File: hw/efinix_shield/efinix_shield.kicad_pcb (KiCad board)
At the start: 2 copper layers, 12 parts, among them J1 DB15_Female_HighDensity_Mount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, J3 Conn_02x18_Odd_Even, U1 MAX3421E, U2 CP2102N-Axx-xQFN24

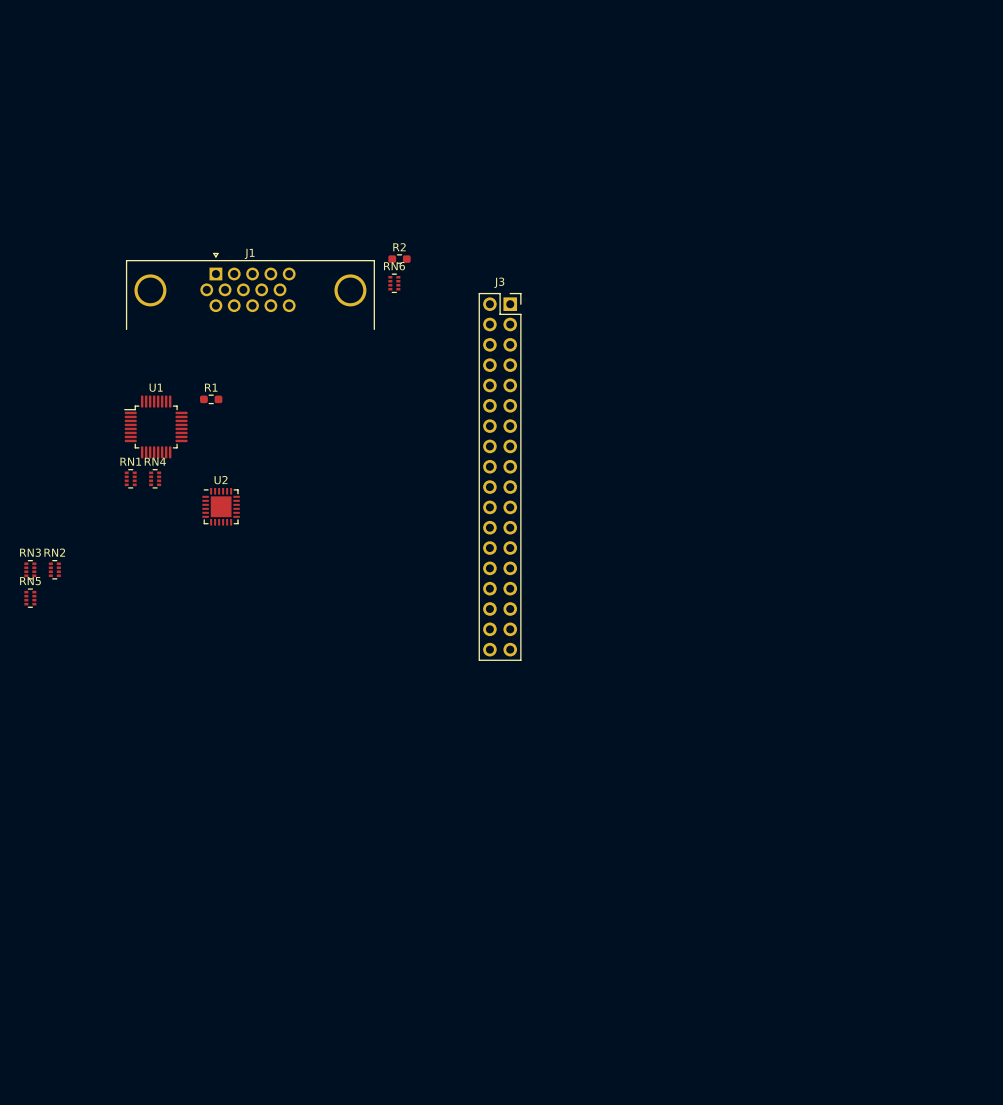
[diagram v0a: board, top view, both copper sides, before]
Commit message: throw some stuff on.
This will have to be changed, some things like the VGA connector will
not work because they will interfere with the cpu adapter.

It may be worth thinking about making these smaller and not including
the ethernet for example, since that will not come for a while.

The only things we really need to start are the SD card and serial port.
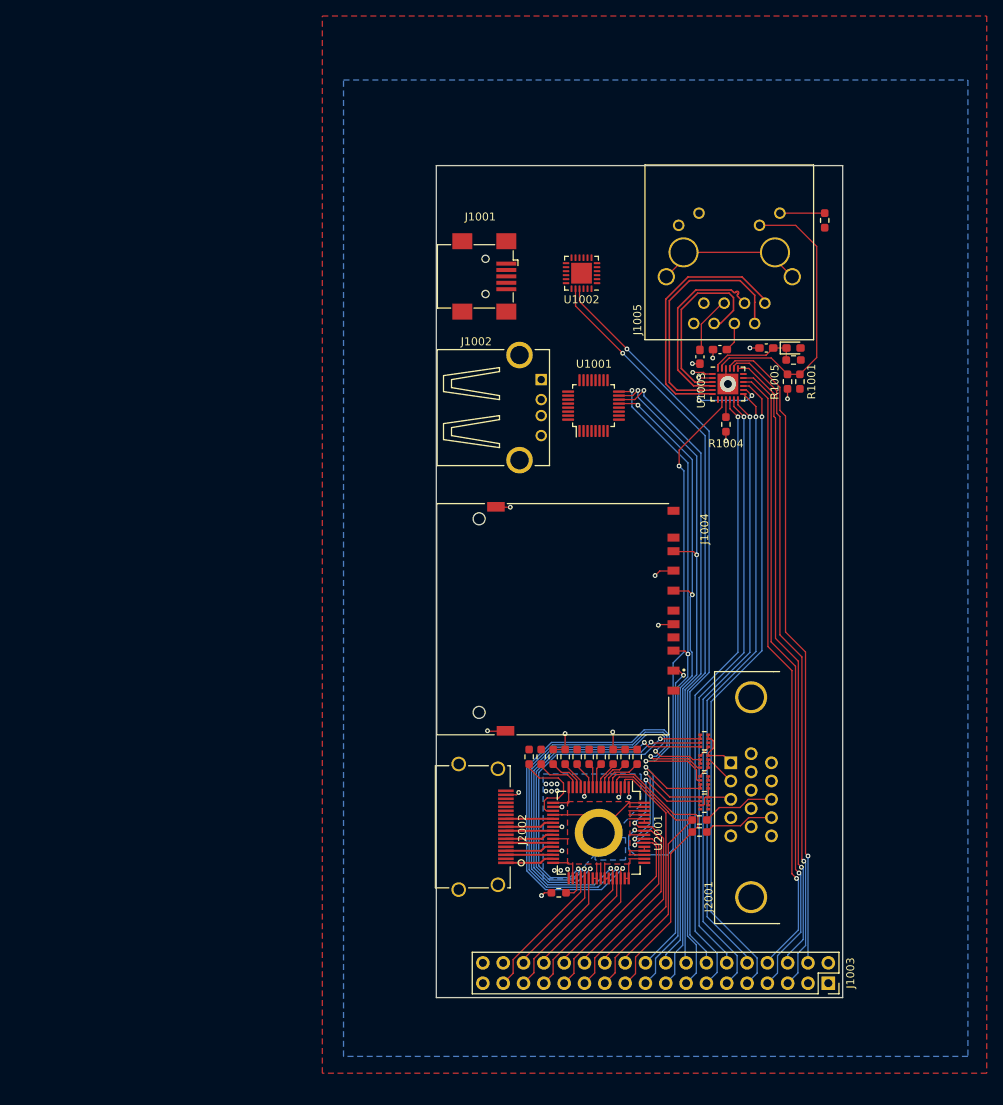
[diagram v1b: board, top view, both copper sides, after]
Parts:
- removed J1: DB15_Female_HighDensity_MountingHoles, Connector_Dsub:DSUB-15-HD_Male_Horizontal_P2.29x1.98mm_EdgePinOffset3.03mm_Housed_MountingHolesOffset4.94mm
- removed R1, R2: 120, Resistor_SMD:R_0603_1608Metric_Pad0.98x0.95mm_HandSolder
- removed RN1, RN2, RN5: 1k, Resistor_SMD:R_Array_Concave_4x0402
- removed RN3, RN4, RN6: 2k, Resistor_SMD:R_Array_Concave_4x0402
- added C1001: 0.1u, Capacitor_SMD:C_0603_1608Metric_Pad1.08x0.95mm_HandSolder, F.Cu at (193.9, 71.4)
- added C1002: 0.1u, Capacitor_SMD:C_0603_1608Metric_Pad1.08x0.95mm_HandSolder, F.Cu at (196.4, 70.5)
- added C1003: 10u, Capacitor_SMD:C_0603_1608Metric_Pad1.08x0.95mm_HandSolder, F.Cu at (202.2, 70.3)
- added D1001: 1N4148, Diode_SMD:D_0603_1608Metric_Pad1.05x0.95mm_HandSolder, F.Cu at (205.7, 70.3)
- added J1001: USB_B_Mini, Connector_USB:USB_Mini-B_Wuerth_65100516121_Horizontal, F.Cu at (167.2, 61.4)
- added J1002: USB_A, Connector_USB:FCI_87520-0010BLF, F.Cu at (171.4, 77.8)
- added J1004: 10067847-001RLF, Connector_Card:AMPHENOL_10067847-001RLF, F.Cu at (166.3, 103.8)
- added J1005: JX0011D21NL, Connector_RJ:JX0011D21NL, F.Cu at (202.1, 64.7)
- added J2001: VGA, Connector_Dsub:ICD15S13E4GX00LF, F.Cu at (200.4, 138.9)
- added J2002: HDMI_A, Connector_HDMI:10029449-111RLF, F.Cu at (169.7, 134.7)
- added R1001: 4k7, Resistor_SMD:R_0603_1608Metric_Pad0.98x0.95mm_HandSolder, F.Cu at (206.4, 74.5)
- added R1002: 10k, Resistor_SMD:R_0603_1608Metric_Pad0.98x0.95mm_HandSolder, F.Cu at (205.7, 71.8)
- added R1003: 220, Resistor_SMD:R_0603_1608Metric_Pad0.98x0.95mm_HandSolder, F.Cu at (209.6, 54.4)
- added R1004: 6.49k 1%, Resistor_SMD:R_0603_1608Metric_Pad0.98x0.95mm_HandSolder, F.Cu at (197.2, 79.8)
- added R1005: 1k, Resistor_SMD:R_0603_1608Metric_Pad0.98x0.95mm_HandSolder, F.Cu at (204.9, 74.5)
- added R2001: 500, Resistor_SMD:R_0603_1608Metric_Pad0.98x0.95mm_HandSolder, F.Cu at (172.6, 121.4)
- added R2002: 120, Resistor_SMD:R_0603_1608Metric_Pad0.98x0.95mm_HandSolder, F.Cu at (193.9, 129.3)
- added R2003: 120, Resistor_SMD:R_0603_1608Metric_Pad0.98x0.95mm_HandSolder, F.Cu at (193.9, 130.8)
- added R2004: 10k, Resistor_SMD:R_0603_1608Metric_Pad0.98x0.95mm_HandSolder, F.Cu at (181.6, 121.4)
- added R2005: 10k, Resistor_SMD:R_0603_1608Metric_Pad0.98x0.95mm_HandSolder, F.Cu at (176.3, 138.4)
- added R2006: 10k, Resistor_SMD:R_0603_1608Metric_Pad0.98x0.95mm_HandSolder, F.Cu at (178.6, 121.4)
- added R2007: 10k, Resistor_SMD:R_0603_1608Metric_Pad0.98x0.95mm_HandSolder, F.Cu at (180.1, 121.4)
- added R2008: 10k, Resistor_SMD:R_0603_1608Metric_Pad0.98x0.95mm_HandSolder, F.Cu at (177.1, 121.4)
- added R2009: 10k, Resistor_SMD:R_0603_1608Metric_Pad0.98x0.95mm_HandSolder, F.Cu at (183.1, 121.4)
- added R2010: 10k, Resistor_SMD:R_0603_1608Metric_Pad0.98x0.95mm_HandSolder, F.Cu at (184.6, 121.4)
- added R2011: 10k, Resistor_SMD:R_0603_1608Metric_Pad0.98x0.95mm_HandSolder, F.Cu at (186.1, 121.4)
- added R2012: 10k, Resistor_SMD:R_0603_1608Metric_Pad0.98x0.95mm_HandSolder, F.Cu at (174.1, 121.4)
- added R2013: 10k, Resistor_SMD:R_0603_1608Metric_Pad0.98x0.95mm_HandSolder, F.Cu at (175.6, 121.4)
- added RN2001: 1k, Resistor_SMD:R_Array_Concave_4x0402, F.Cu at (194.5, 119.4)
- added RN2002: 1k, Resistor_SMD:R_Array_Concave_4x0402, F.Cu at (194.5, 122.0)
- added RN2003: 1k, Resistor_SMD:R_Array_Concave_4x0402, F.Cu at (194.5, 124.6)
- added RN2004: 1k, Resistor_SMD:R_Array_Concave_4x0402, F.Cu at (194.5, 127.2)
- added U1003: KSZ8081RNA, Package_DFN_QFN:QFN-24-1EP_4x4mm_P0.5mm_EP2.6x2.6mm, F.Cu at (197.4, 74.8)
- added U2001: TFP410PAP, Package_QFP:HTQFP-64-1EP_10x10mm_P0.5mm_EP8x8mm_Mask4.4x4.4mm_ThermalVias, F.Cu at (181.3, 130.9)
- moved J1003 93.7 mm to (210.0, 149.7), turned to -90 degrees
- moved U1001 54.7 mm to (180.7, 77.5), turned to 90 degrees
- moved U1002 53.7 mm to (179.2, 61.0), turned to 180 degrees
- renumbered J3 to J1003, U1 to U1001, U2 to U1002
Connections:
- net VDD renamed +3V3
- J1003 pad 10: unconnected-(J3-Pad10) -> /RMII_RXD0
- J1003 pad 11: unconnected-(J3-Pad11) -> /RMII_RXD1
- J1003 pad 12: unconnected-(J3-Pad12) -> /MDCLK
- J1003 pad 13: unconnected-(J3-Pad13) -> /MDIO
- J1003 pad 14: unconnected-(J3-Pad14) -> /UART_RX
- J1003 pad 15: unconnected-(J3-Pad15) -> /UART_TX
- J1003 pad 16: unconnected-(J3-Pad16) -> /SPI_USB_CS
- J1003 pad 17: unconnected-(J3-Pad17) -> /SPI_MISO
- J1003 pad 18: unconnected-(J3-Pad18) -> /SPI_CLK
- J1003 pad 19: unconnected-(J3-Pad19) -> /SPI_MOSI
- J1003 pad 20: unconnected-(J3-Pad20) -> /SPI_SD_CS
- J1003 pad 21: unconnected-(J3-Pad21) -> /VGA_VS
- J1003 pad 22: unconnected-(J3-Pad22) -> /VGA_HS
- J1003 pad 23: unconnected-(J3-Pad23) -> /DVI_DE
- J1003 pad 24: unconnected-(J3-Pad24) -> /VGA_BLUE_0
- J1003 pad 25: unconnected-(J3-Pad25) -> /DVI_CLK
- J1003 pad 26: unconnected-(J3-Pad26) -> /VGA_BLUE_1
- J1003 pad 27: unconnected-(J3-Pad27) -> /VGA_BLUE_2
- J1003 pad 28: unconnected-(J3-Pad28) -> /VGA_GREEN_0
- J1003 pad 29: unconnected-(J3-Pad29) -> /VGA_GREEN_1
- J1003 pad 3: unconnected-(J3-Pad3) -> /SPI_CS_3
- J1003 pad 30: unconnected-(J3-Pad30) -> /VGA_GREEN_2
- J1003 pad 31: unconnected-(J3-Pad31) -> /VGA_RED_0
- J1003 pad 32: unconnected-(J3-Pad32) -> /VGA_RED_1
- J1003 pad 33: unconnected-(J3-Pad33) -> /VGA_RED_2
- J1003 pad 4: unconnected-(J3-Pad4) -> /RMII_TXD1
- J1003 pad 5: unconnected-(J3-Pad5) -> /RMII_TXD0
- J1003 pad 6: unconnected-(J3-Pad6) -> /RMII_TX_EN
- J1003 pad 7: unconnected-(J3-Pad7) -> /RMII_RX_ERR
- J1003 pad 8: unconnected-(J3-Pad8) -> /RMII_CLK_REF
- J1003 pad 9: unconnected-(J3-Pad9) -> /RMII_CRS_DV
- U1001 pad 13: unconnected-(U1-Pad13) -> /SPI_CLK
- U1001 pad 14: unconnected-(U1-Pad14) -> /SPI_USB_CS
- U1001 pad 15: unconnected-(U1-Pad15) -> /SPI_MISO
- U1001 pad 16: unconnected-(U1-Pad16) -> /SPI_MOSI
- U1002 pad 20: unconnected-(U2-Pad20) -> /UART_TX
- U1002 pad 21: unconnected-(U2-Pad21) -> /UART_RX
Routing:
- net /UART_TX: track 0.00 -> 95.4 mm, vias 0 -> 1
- net /DVI_CLK: track 0.00 -> 93.6 mm, vias 0 -> 2
- net /UART_RX: track 0.00 -> 92.8 mm, vias 0 -> 1
- net /SPI_MISO: track 0.00 -> 84.5 mm, vias 0 -> 2
- net /RMII_TXD0: track 0.00 -> 83.7 mm, vias 0 -> 1
- net /SPI_MOSI: track 0.00 -> 82.9 mm, vias 0 -> 2
- net /RMII_TXD1: track 0.00 -> 81.6 mm, vias 0 -> 1
- net /RMII_CRS_DV: track 0.00 -> 81.6 mm, vias 0 -> 1
- net /RMII_RX_ERR: track 0.00 -> 81.1 mm, vias 0 -> 1
- net /RMII_TX_EN: track 0.00 -> 79.3 mm, vias 0 -> 1
- net /SPI_CLK: track 0.00 -> 79.1 mm, vias 0 -> 2
- net /SPI_USB_CS: track 0.00 -> 79.0 mm, vias 0 -> 1
- net /RMII_RXD1: track 0.00 -> 78.3 mm, vias 0 -> 1
- net /RMII_CLK_REF: track 0.00 -> 77.7 mm, vias 0 -> 1
- net /MDIO: track 0.00 -> 77.3 mm, vias 0 -> 1
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- added copper zone on B.Cu, net +3V3
- added copper zone on F.Cu, net +3V3
- added copper zone on B.Cu, net GND
- added copper zone on F.Cu, net GND
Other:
- board outline added: 50.8 x 104 mm

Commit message: Start work on simpler board
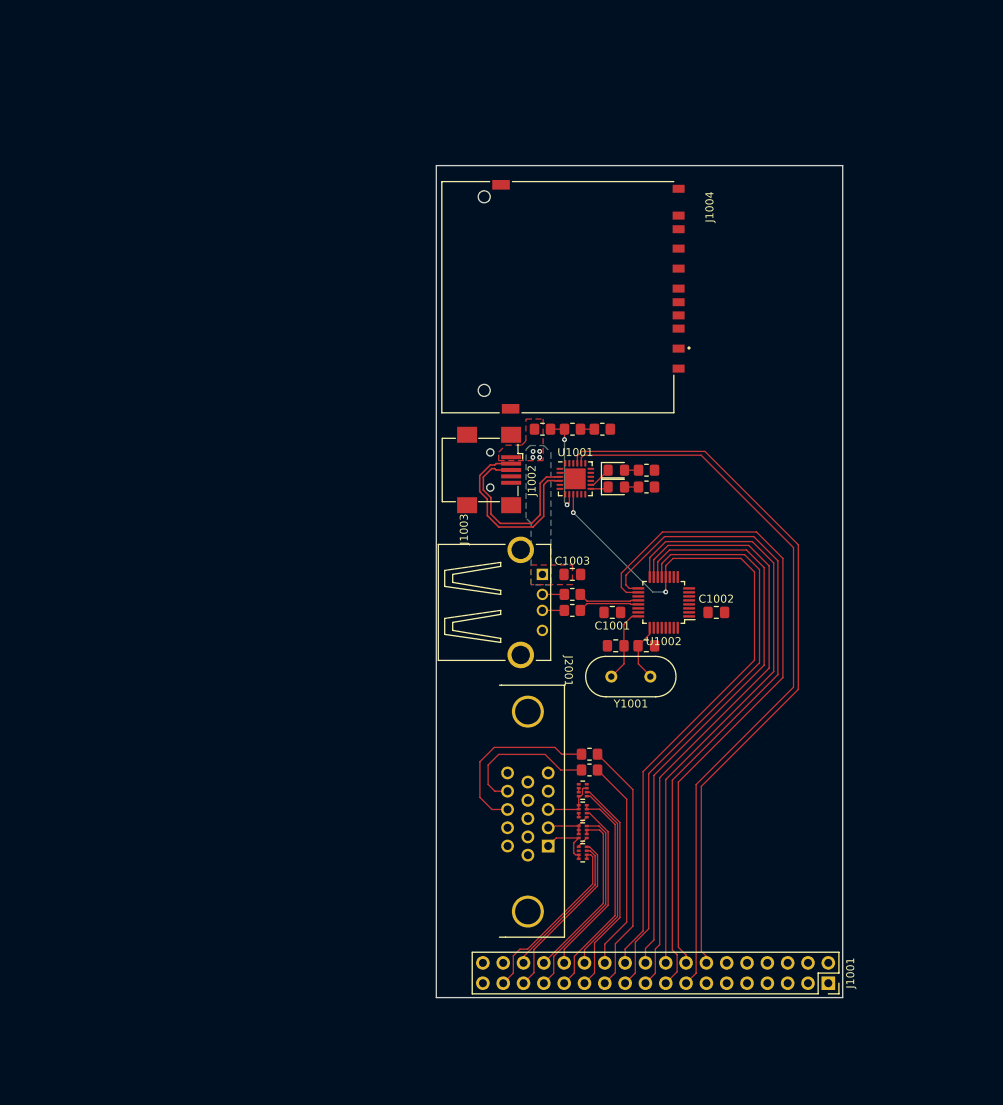
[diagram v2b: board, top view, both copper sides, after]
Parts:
- removed the J1001 at (167.2, 61.4)
- removed J1005: JX0011D21NL, Connector_RJ:JX0011D21NL
- removed J2002: HDMI_A, Connector_HDMI:10029449-111RLF
- removed R2003: 120, Resistor_SMD:R_0603_1608Metric_Pad0.98x0.95mm_HandSolder
- removed R2004, R2005, R2006, R2007, R2008, R2009, R2010, R2011, R2012, R2013: 10k, Resistor_SMD:R_0603_1608Metric_Pad0.98x0.95mm_HandSolder
- removed U1003: KSZ8081RNA, Package_DFN_QFN:QFN-24-1EP_4x4mm_P0.5mm_EP2.6x2.6mm
- removed U2001: TFP410PAP, Package_QFP:HTQFP-64-1EP_10x10mm_P0.5mm_EP8x8mm_Mask4.4x4.4mm_ThermalVias
- added C1004: C, Capacitor_SMD:C_0805_2012Metric_Pad1.18x1.45mm_HandSolder, F.Cu at (183.4, 107.5)
- added C1005: C, Capacitor_SMD:C_0805_2012Metric_Pad1.18x1.45mm_HandSolder, F.Cu at (187.2, 107.5)
- added D1002: GRN, LED_SMD:LED_0805_2012Metric_Pad1.15x1.40mm_HandSolder, F.Cu at (183.5, 87.7)
- added J1003: USB_A, Connector_USB:FCI_87520-0010BLF, F.Cu at (171.6, 102.1)
- added R1006: 33, Resistor_SMD:R_0805_2012Metric_Pad1.20x1.40mm_HandSolder, F.Cu at (178.0, 101.1)
- added R1007: 33, Resistor_SMD:R_0805_2012Metric_Pad1.20x1.40mm_HandSolder, F.Cu at (178.0, 103.1)
- added Y1001: 12MHz, Crystal:Crystal_HC49-U_Vertical, F.Cu at (182.9, 111.4)
- C1001: value 0.1u -> 1u; footprint Capacitor_SMD:C_0603_1608Metric_Pad1.08x0.95mm_HandSolder -> Capacitor_SMD:C_0805_2012Metric_Pad1.18x1.45mm_HandSolder
- C1002: footprint Capacitor_SMD:C_0603_1608Metric_Pad1.08x0.95mm_HandSolder -> Capacitor_SMD:C_0805_2012Metric_Pad1.18x1.45mm_HandSolder
- C1003: value 10u -> 4.7u; footprint Capacitor_SMD:C_0603_1608Metric_Pad1.08x0.95mm_HandSolder -> Capacitor_SMD:C_0805_2012Metric_Pad1.18x1.45mm_HandSolder
- D1001: value 1N4148 -> RED; footprint Diode_SMD:D_0603_1608Metric_Pad1.05x0.95mm_HandSolder -> LED_SMD:LED_0805_2012Metric_Pad1.15x1.40mm_HandSolder
- J1002: value USB_A -> USB_B_Mini; footprint Connector_USB:FCI_87520-0010BLF -> Connector_USB:USB_Mini-B_Wuerth_65100516121_Horizontal
- R1001: value 4k7 -> 10k; footprint Resistor_SMD:R_0603_1608Metric_Pad0.98x0.95mm_HandSolder -> Resistor_SMD:R_0805_2012Metric_Pad1.20x1.40mm_HandSolder
- R1002, R1005, R2002: footprint Resistor_SMD:R_0603_1608Metric_Pad0.98x0.95mm_HandSolder -> Resistor_SMD:R_0805_2012Metric_Pad1.20x1.40mm_HandSolder
- R1003: value 220 -> 10k; footprint Resistor_SMD:R_0603_1608Metric_Pad0.98x0.95mm_HandSolder -> Resistor_SMD:R_0805_2012Metric_Pad1.20x1.40mm_HandSolder
- R1004: value 6.49k 1% -> 1k; footprint Resistor_SMD:R_0603_1608Metric_Pad0.98x0.95mm_HandSolder -> Resistor_SMD:R_0805_2012Metric_Pad1.20x1.40mm_HandSolder
- R2001: value 500 -> 120; footprint Resistor_SMD:R_0603_1608Metric_Pad0.98x0.95mm_HandSolder -> Resistor_SMD:R_0805_2012Metric_Pad1.20x1.40mm_HandSolder
- U1001: value MAX3421E -> CP2102N-Axx-xQFN24; footprint Package_QFP:LQFP-32_5x5mm_P0.5mm -> Package_DFN_QFN:QFN-24-1EP_4x4mm_P0.5mm_EP2.6x2.6mm
- U1002: value CP2102N-Axx-xQFN24 -> MAX3421E; footprint Package_DFN_QFN:QFN-24-1EP_4x4mm_P0.5mm_EP2.6x2.6mm -> Package_QFP:LQFP-32_5x5mm_P0.5mm
- moved U1002 42.4 mm to (189.4, 102.1)
- moved J1004 40.3 mm to (167.0, 63.5)
- moved R1003 38.1 mm to (181.8, 80.5), turned to 0 degrees
- moved C1003 37.3 mm to (178.0, 98.6), turned to 0 degrees
- moved J2001 36.3 mm to (172.4, 115.8), turned to -90 degrees
- moved C1001 33.8 mm to (183.0, 103.3), turned to 180 degrees
- moved C1002 32.9 mm to (196.0, 103.3)
- moved R1001 32.7 mm to (174.3, 80.5), turned to 0 degrees
- moved R1002 28.9 mm to (178.0, 80.5), turned to 0 degrees
- moved D1001 26.9 mm to (183.5, 85.6)
- moved R1005 22.0 mm to (187.3, 87.7), turned to 180 degrees
- moved RN2001 20.7 mm to (179.3, 133.4), turned to 180 degrees
- moved RN2002 17.6 mm to (179.3, 130.8), turned to 180 degrees
- moved RN2003 15.6 mm to (179.3, 128.2), turned to 180 degrees
- moved RN2004 15.3 mm to (179.3, 125.6), turned to 180 degrees
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- renumbered J1003 to J1001
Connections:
- C1001 pad 1: GND -> +3V3
- C1001 pad 2: Net-(C1001-Pad2) -> GND
- C1002 pad 1: GND -> +3V3
- C1002 pad 2: Net-(C1002-Pad2) -> GND
- C1003 pad 1: /~{PHY_RST} -> +5V
- D1001 pad 1: /~{PHY_RST} -> /TX_LED
- D1001 pad 2: +3V3 -> Net-(D1001-Pad2)
- J1001 pad 10: /RMII_RXD0 -> unconnected-(J1001-Pad10)
- J1001 pad 11: /RMII_RXD1 -> unconnected-(J1001-Pad11)
- J1001 pad 12: /MDCLK -> unconnected-(J1001-Pad12)
- J1001 pad 13: /MDIO -> unconnected-(J1001-Pad13)
- J1001 pad 16: /SPI_USB_CS -> /USB_INT
- J1001 pad 17: /SPI_MISO -> /USB_GPX
- J1001 pad 18: /SPI_CLK -> /SPI_MOSI
- J1001 pad 19: /SPI_MOSI -> /SPI_MISO
- J1001 pad 20: /SPI_SD_CS -> /SPI_USB_CS
- J1001 pad 21: /VGA_VS -> /SPI_CLK
- J1001 pad 22: /VGA_HS -> /~{RESET}
- J1001 pad 23: /DVI_DE -> /VGA_HS
- J1001 pad 24: /VGA_BLUE_0 -> /VGA_VS
- J1001 pad 25: /DVI_CLK -> /VGA_BLUE_0
- J1001 pad 3: /SPI_CS_3 -> unconnected-(J1001-Pad3)
- J1001 pad 4: /RMII_TXD1 -> unconnected-(J1001-Pad4)
- J1001 pad 5: /RMII_TXD0 -> unconnected-(J1001-Pad5)
- J1001 pad 6: /RMII_TX_EN -> unconnected-(J1001-Pad6)
- J1001 pad 7: /RMII_RX_ERR -> unconnected-(J1001-Pad7)
- J1001 pad 8: /RMII_CLK_REF -> unconnected-(J1001-Pad8)
- J1001 pad 9: /RMII_CRS_DV -> unconnected-(J1001-Pad9)
- J1002 pad 1: unconnected-(J1002-Pad1) -> +5V
- J1002 pad 2: unconnected-(J1002-Pad2) -> /USBB_DN
- J1002 pad 3: unconnected-(J1002-Pad3) -> /USBB_DP
- J1004 pad 1: /SPI_SD_CS -> /SD_D3
- J1004 pad 2: /SPI_MOSI -> /SD_CMD
- J1004 pad 5: /SPI_CLK -> /SD_CLK
- J1004 pad 7: /SPI_MISO -> /SD_D0
- J1004 pad 8: unconnected-(J1004-Pad8) -> /SD_D1
- J1004 pad 9: unconnected-(J1004-Pad9) -> /SD_D2
- R1001 pad 1: +3V3 -> +5V
- R1001 pad 2: Net-(U1003-Pad23) -> Net-(R1001-Pad2)
- R1002 pad 1: +3V3 -> Net-(R1001-Pad2)
- R1002 pad 2: /~{PHY_RST} -> Net-(R1002-Pad2)
- R1003 pad 1: +3V3 -> Net-(R1002-Pad2)
- R1003 pad 2: Net-(J1005-Pad9) -> GND
- R1004 pad 1: Net-(U1003-Pad9) -> +3V3
- R1004 pad 2: GND -> Net-(D1001-Pad2)
- R1005 pad 1: Net-(U1003-Pad23) -> +3V3
- R1005 pad 2: GND -> Net-(D1002-Pad2)
- R2001 pad 1: Net-(R2001-Pad1) -> /VGA_HS
- R2001 pad 2: +3V3 -> Net-(J2001-Pad13)
- R2002 pad 1: /VGA_HS -> /VGA_VS
- R2002 pad 2: Net-(J2001-Pad13) -> Net-(J2001-Pad14)
- RN2001 pad 6: unconnected-(RN2001-Pad6) -> /video/VGA_RED
- U1001 pad 13: /SPI_CLK -> /RX_LED
- U1001 pad 14: /SPI_USB_CS -> /TX_LED
- U1001 pad 15: /SPI_MISO -> unconnected-(U1001-Pad15)
- U1001 pad 16: /SPI_MOSI -> unconnected-(U1001-Pad16)
- U1001 pad 2: unconnected-(U1001-Pad2) -> GND
- U1001 pad 20: unconnected-(U1001-Pad20) -> /UART_TX
- U1001 pad 21: unconnected-(U1001-Pad21) -> /UART_RX
- U1001 pad 25: unconnected-(U1001-Pad25) -> GND
- U1001 pad 3: unconnected-(U1001-Pad3) -> /USBB_DP
- U1001 pad 4: unconnected-(U1001-Pad4) -> /USBB_DN
- U1001 pad 5: unconnected-(U1001-Pad5) -> +3V3
- U1001 pad 6: unconnected-(U1001-Pad6) -> +3V3
- U1001 pad 7: unconnected-(U1001-Pad7) -> +3V3
- U1001 pad 8: unconnected-(U1001-Pad8) -> Net-(R1001-Pad2)
- U1001 pad 9: unconnected-(U1001-Pad9) -> /~{RESET}
- U1002 pad 12: unconnected-(U1002-Pad12) -> /~{RESET}
- U1002 pad 13: unconnected-(U1002-Pad13) -> /SPI_CLK
- U1002 pad 14: unconnected-(U1002-Pad14) -> /SPI_USB_CS
- U1002 pad 15: unconnected-(U1002-Pad15) -> /SPI_MISO
- U1002 pad 16: unconnected-(U1002-Pad16) -> /SPI_MOSI
- U1002 pad 17: unconnected-(U1002-Pad17) -> /USB_GPX
- U1002 pad 18: unconnected-(U1002-Pad18) -> /USB_INT
- U1002 pad 19: unconnected-(U1002-Pad19) -> GND
- U1002 pad 2: Net-(U1002-Pad2) -> +3V3
- U1002 pad 20: /UART_TX -> Net-(R1006-Pad1)
- U1002 pad 21: /UART_RX -> Net-(R1007-Pad2)
- U1002 pad 23: unconnected-(U1002-Pad23) -> +3V3
- U1002 pad 24: unconnected-(U1002-Pad24) -> Net-(C1004-Pad1)
- U1002 pad 25: Net-(U1002-Pad2) -> Net-(C1005-Pad1)
- U1002 pad 3: unconnected-(U1002-Pad3) -> GND
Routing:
- net /DVI_CLK: track 93.6 -> 0.00 mm, vias 2 -> 0
- net /~{RESET}: track 0.00 -> 89.0 mm, vias 0 -> 2
- net /USB_GPX: track 0.00 -> 84.3 mm
- net /USB_INT: track 0.00 -> 84.2 mm
- net /RMII_TXD0: track 83.7 -> 0.00 mm, vias 1 -> 0
- net /RMII_TXD1: track 81.6 -> 0.00 mm, vias 1 -> 0
- net /RMII_CRS_DV: track 81.6 -> 0.00 mm, vias 1 -> 0
- net /RMII_RX_ERR: track 81.1 -> 0.00 mm, vias 1 -> 0
- net /RMII_TX_EN: track 79.3 -> 0.00 mm, vias 1 -> 0
- net /RMII_RXD1: track 78.3 -> 0.00 mm, vias 1 -> 0
- net /RMII_CLK_REF: track 77.7 -> 0.00 mm, vias 1 -> 0
- net /MDIO: track 77.3 -> 0.00 mm, vias 1 -> 0
- net /RMII_RXD0: track 76.4 -> 0.00 mm, vias 1 -> 0
- net /MDCLK: track 74.7 -> 0.00 mm, vias 1 -> 0
- net GND: track 73.5 -> 2.25 mm, vias 13 -> 0
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- added copper zone on B.Cu, net +5V
- added copper zone on F.Cu, net +5V
- removed copper zone on B.Cu, net +3V3
- removed copper zone on F.Cu, net +3V3
- removed copper zone on B.Cu, net GND
- removed copper zone on F.Cu, net GND

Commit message: Finish routing sd card slot, update gitignore
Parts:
- added J1001: Conn_01x06, Connector_PinHeader_2.54mm:PinHeader_1x06_P2.54mm_Vertical, F.Cu at (197.9, 74.8)
- added R1001: 0, Resistor_SMD:R_0805_2012Metric_Pad1.20x1.40mm_HandSolder, F.Cu at (194.9, 79.5)
- added R1002: 10k, Resistor_SMD:R_0805_2012Metric_Pad1.20x1.40mm_HandSolder, F.Cu at (191.9, 82.5)
- added R1003: 0, Resistor_SMD:R_0805_2012Metric_Pad1.20x1.40mm_HandSolder, F.Cu at (192.0, 84.6)
- added R1004: 10k, Resistor_SMD:R_0805_2012Metric_Pad1.20x1.40mm_HandSolder, F.Cu at (200.8, 81.4)
- added R1005: 10k, Resistor_SMD:R_0805_2012Metric_Pad1.20x1.40mm_HandSolder, F.Cu at (200.8, 77.7)
- moved C1002 1.11 mm to (194.9, 103.2), turned to 90 degrees
- renumbered J1001 to J1002, J1002 to J1003, J1003 to J1004, J1004 to J1005, R1001 to R1006, R1002 to R1007, R1003 to R1008, R1004 to R1009, R1005 to R1010, R1006 to R1011, R1007 to R1012
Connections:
- J1002 pad 10: unconnected-(J1001-Pad10) -> /SD_CLK
- J1002 pad 11: unconnected-(J1001-Pad11) -> /SD_CMD
- J1002 pad 12: unconnected-(J1001-Pad12) -> /SD_D3
- J1002 pad 13: unconnected-(J1001-Pad13) -> /SD_D2
- J1002 pad 8: unconnected-(J1001-Pad8) -> /SD_D1
- J1002 pad 9: unconnected-(J1001-Pad9) -> /SD_D0
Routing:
- net /SD_D0: track 0.00 -> 107.5 mm
- net /SD_D1: track 0.00 -> 106.2 mm
- net /SD_CLK: track 0.00 -> 101.1 mm
- net /SD_CMD: track 0.00 -> 100.4 mm
- net /SD_D2: track 0.00 -> 97.0 mm
- net /SD_D3: track 0.00 -> 95.6 mm
- net +5V: track 0.00 -> 22.9 mm, vias 4 -> 5
- net +3V3: track 0.00 -> 12.0 mm, vias 0 -> 9
- net /HOST_TX: track 0.00 -> 7.86 mm
- net /HOST_RX: track 0.00 -> 5.05 mm
- net /~{RESET}: track 89.0 -> 84.1 mm
- net /SPI_CLK: track 73.8 -> 69.0 mm
- net /SPI_USB_CS: track 72.3 -> 67.7 mm
- net /SPI_MISO: track 77.0 -> 72.5 mm
- net /SPI_MOSI: track 75.4 -> 71.1 mm
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- added copper zone on B.Cu, net +3V3
- added copper zone on F.Cu, net +3V3
- added copper zone on B.Cu, net GND
- added copper zone on F.Cu, net GND
